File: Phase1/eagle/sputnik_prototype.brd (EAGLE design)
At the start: 100 x 80 mm, 82 parts, among them U1 MEGA128-M, U2 MIC5219 3.3V, Y1 32MHz, Y2 8MHZ

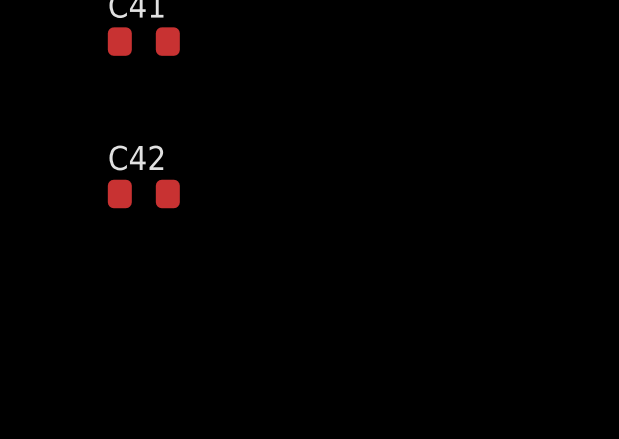
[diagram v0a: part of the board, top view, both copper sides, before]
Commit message: Updated RF schematic
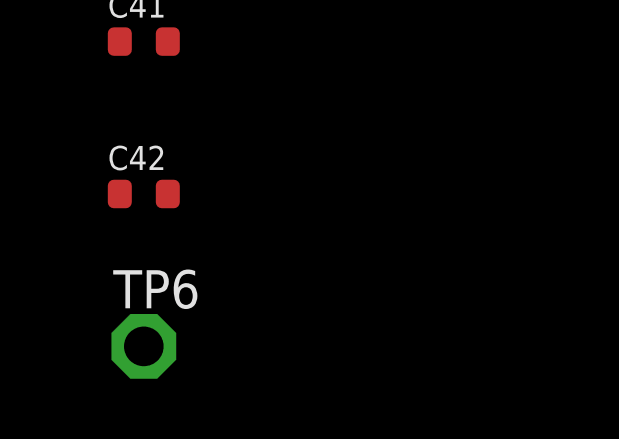
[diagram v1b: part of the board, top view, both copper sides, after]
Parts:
- added TP6: TPSPAD1-13, testpad:P1-13
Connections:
- removed net N$26: C13.1, U$5.2
- removed net N$33: C23.1, C4.1, C6.1, L2.2
- new net N$4: C13.1, L8.1, U$4.6
- new net N$5: C23.1, U$5.8
- net GND: no longer U$4.1
- net N$22: now also U$5.2; no longer U$5.8
- net RFIO: now also C4.1, C6.1, L2.2; no longer L8.1, U$4.6
- net V+: now also TP6.TP
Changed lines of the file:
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@@
 <?xml version="1.0" encoding="utf-8"?>
 <!DOCTYPE eagle SYSTEM "eagle.dtd">
-<eagle version="7.3.0">
+<eagle version="7.5.0">
 <drawing>
 <settings>
@@
 <element name="C41" library="rcl_custom" package=".0603-B-NOSILK" value="100nF" x="-55.88" y="-101.6"/>
 <element name="C42" library="rcl_custom" package=".0603-B-NOSILK" value="470pF" x="-55.88" y="-106.68"/>
+<element name="TP6" library="testpad" package="P1-13" value="TPSPAD1-13" x="-55.88" y="-111.76">
+<attribute name="TP_SIGNAL_NAME" value="" x="-55.88" y="-111.76" size="1.778" layer="27" display="off"/>
+</element>
 </elements>
 <signals>
@@
 <contactref element="U$4" pad="2"/>
 <contactref element="U$4" pad="5"/>
-<contactref element="U$4" pad="1"/>
 <contactref element="C25" pad="2"/>
 <contactref element="C24" pad="2"/>
-<contactref element="U$5" pad="6"/>
 <contactref element="U$5" pad="7"/>
 <contactref element="U$5" pad="9"/>
-<contactref element="U$5" pad="4"/>
 <contactref element="U$5" pad="3"/>
 <contactref element="U$5" pad="1"/>
@@
 <contactref element="U2" pad="2"/>
 <contactref element="C42" pad="1"/>
+<contactref element="U$5" pad="4"/>
+<contactref element="U$5" pad="6"/>
 <wire x1="-56.68" y1="-101.6" x2="-56.68" y2="-106.68" width="0" layer="19" extent="1-1"/>
 <wire x1="-56.68" y1="-96.52" x2="-56.68" y2="-101.6" width="0" layer="19" extent="1-1"/>
@@
 <wire x1="-22.06" y1="48.26" x2="-19.85" y2="44.45" width="0" layer="19" extent="1-1"/>
 <wire x1="-22.86" y1="51.1975" x2="-22.06" y2="48.26" width="0" layer="19" extent="1-1"/>
-<wire x1="-23.51" y1="51.1975" x2="-22.86" y2="51.1975" width="0" layer="19" extent="1-1"/>
 <wire x1="-22.86" y1="52.8725" x2="-22.86" y2="51.1975" width="0" layer="19" extent="1-1"/>
-<wire x1="-25.87" y1="48.26" x2="-23.51" y2="51.1975" width="0" layer="19" extent="1-1"/>
+<wire x1="-25.87" y1="48.26" x2="-22.06" y2="48.26" width="0" layer="19" extent="1-1"/>
 <wire x1="-23.241" y1="32.258" x2="-22.39" y2="36.83" width="0" layer="19" extent="1-1"/>
 <wire x1="-23.241" y1="32.258" x2="-23.241" y2="32.258" width="0" layer="19" extent="1-16"/>
@@
 <contactref element="U2" pad="1"/>
 <contactref element="U2" pad="3"/>
+<contactref element="TP6" pad="TP"/>
+<wire x1="-55.08" y1="-101.6" x2="-55.88" y2="-111.76" width="0" layer="19" extent="1-1"/>
 <wire x1="-56.2" y1="-17.8101" x2="-55.08" y2="-101.6" width="0" layer="19" extent="1-1"/>
 <wire x1="-58.1" y1="-17.8101" x2="-56.2" y2="-17.8101" width="0" layer="19" extent="1-1"/>
@@
 </signal>
 <signal name="N$22">
-<contactref element="U$5" pad="8"/>
 <contactref element="U$6" pad="8"/>
-<wire x1="-27.6614" y1="17.3975" x2="-13.26" y2="40.91" width="0" layer="19" extent="1-1"/>
+<contactref element="U$5" pad="2"/>
+<wire x1="-27.6614" y1="17.3975" x2="-15.22" y2="40.91" width="0" layer="19" extent="1-1"/>
 </signal>
 <signal name="N$24">
@@
 <wire x1="-52.54" y1="48.26" x2="-18.25" y2="48.26" width="0" layer="19" extent="1-1"/>
 </signal>
-<signal name="N$26">
-<contactref element="U$5" pad="2"/>
-<contactref element="C13" pad="1"/>
-<wire x1="-23.66" y1="44.45" x2="-15.22" y2="40.91" width="0" layer="19" extent="1-1"/>
-</signal>
 <signal name="N$27">
 <contactref element="U$4" pad="4"/>
@@
 </signal>
 <signal name="RFIO">
-<contactref element="L8" pad="1"/>
-<contactref element="U$4" pad="6"/>
 <contactref element="U$1" pad="39"/>
-<wire x1="-23.51" y1="52.88" x2="-16.04" y2="52.07" width="0" layer="19" extent="1-1"/>
-<wire x1="-25.88" y1="11.4978" x2="-23.51" y2="52.88" width="0" layer="19" extent="1-1"/>
+<contactref element="C6" pad="1"/>
+<contactref element="C4" pad="1"/>
+<contactref element="L2" pad="2"/>
+<wire x1="-30.01" y1="40.64" x2="-25.88" y2="11.4978" width="0" layer="19" extent="1-1"/>
+<wire x1="-37.63" y1="40.64" x2="-30.01" y2="40.64" width="0" layer="19" extent="1-1"/>
+<wire x1="-33.49" y1="48.26" x2="-30.01" y2="40.64" width="0" layer="19" extent="1-1"/>
 </signal>
 <signal name="RXTX">
@@
 <contactref element="U$2" pad="P$3"/>
 <wire x1="-19.05" y1="32.258" x2="-14.24" y2="39.93" width="0" layer="19" extent="1-1"/>
-</signal>
-<signal name="N$33">
-<contactref element="C6" pad="1"/>
-<contactref element="C4" pad="1"/>
-<contactref element="L2" pad="2"/>
-<contactref element="C23" pad="1"/>
-<wire x1="-30.01" y1="40.64" x2="-19.85" y2="48.26" width="0" layer="19" extent="1-1"/>
-<wire x1="-37.63" y1="40.64" x2="-30.01" y2="40.64" width="0" layer="19" extent="1-1"/>
-<wire x1="-33.49" y1="48.26" x2="-30.01" y2="40.64" width="0" layer="19" extent="1-1"/>
 </signal>
 <signal name="N$29">
@@
 <wire x1="-56.2" y1="-15.2099" x2="-55.08" y2="-106.68" width="0" layer="19" extent="1-1"/>
 </signal>
+<signal name="N$4">
+<contactref element="L8" pad="1"/>
+<contactref element="U$4" pad="6"/>
+<contactref element="C13" pad="1"/>
+<wire x1="-23.51" y1="52.88" x2="-16.04" y2="52.07" width="0" layer="19" extent="1-1"/>
+<wire x1="-23.66" y1="44.45" x2="-23.51" y2="52.88" width="0" layer="19" extent="1-1"/>
+</signal>
+<signal name="N$5">
+<contactref element="C23" pad="1"/>
+<contactref element="U$5" pad="8"/>
+<wire x1="-13.26" y1="40.91" x2="-19.85" y2="48.26" width="0" layer="19" extent="1-1"/>
+</signal>
 </signals>

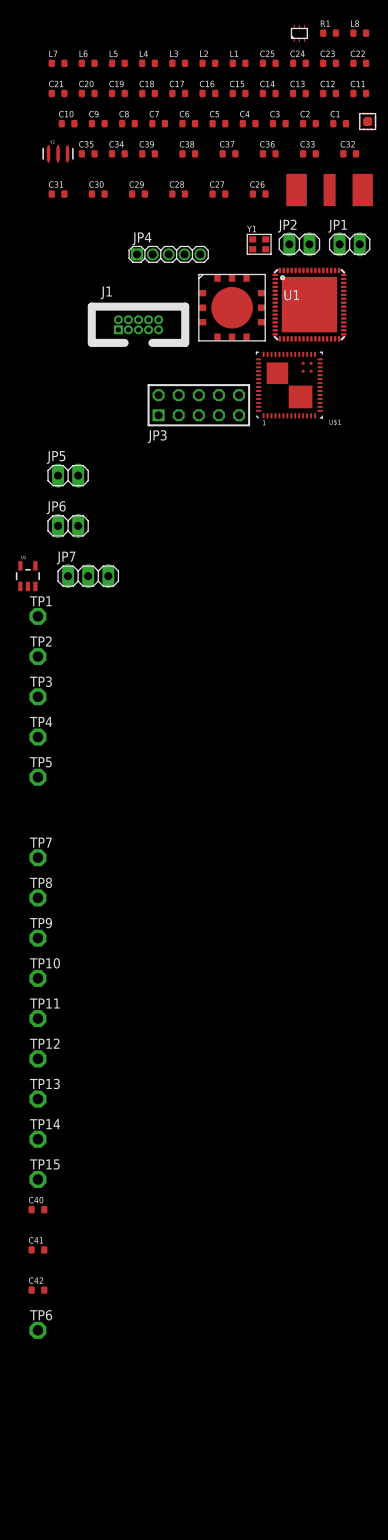
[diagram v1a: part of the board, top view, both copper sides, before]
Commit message: Updated RF schematic
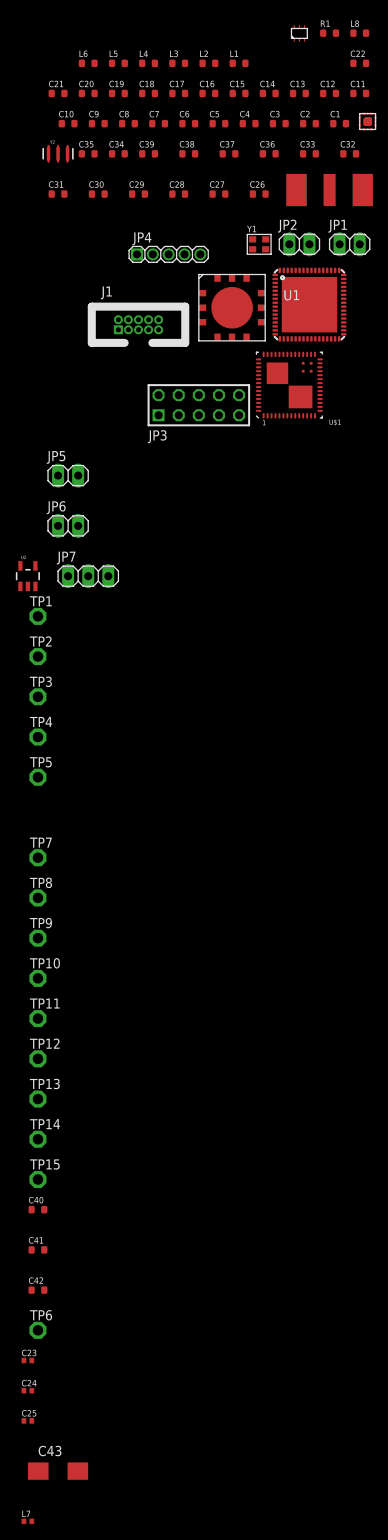
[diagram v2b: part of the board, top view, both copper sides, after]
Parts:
- added C43: 100uF, rcl:CT6032
- C1, C3: value (none) -> 10nF
- C10, C5, C6, C9: value (none) -> 15pF
- C11, C12: value (none) -> 8.2pF
- C13, C14: value (none) -> 100nF
- C15, C17, C19, C22: value (none) -> 10uF
- C16, C18, C20, C21: value (none) -> 0.01uF
- C2, C4: value (none) -> 12pF
- C23, C25: value (none) -> 1nF; device rcl_custom:.0603-B-NOSILK -> rcl_custom:.0402-B-NOSILK
- C24: value (none) -> 10nF; device rcl_custom:.0603-B-NOSILK -> rcl_custom:.0402-B-NOSILK
- C7, C8: value (none) -> 2.2pF
- L1, L2: value (none) -> 22nH
- L3, L4, L5, L6: value (none) -> 15nH
- L7: value (none) -> 24nH; device rcl_custom:.0603-B-NOSILK -> rcl_custom:.0402-B-NOSILK
- L8: value (none) -> 150nH
- R1: value (none) -> 500
- moved L7 184.2 mm to (-57.1, -135.9)
- moved C25 174.1 mm to (-57.1, -123.2)
- moved C24 171.1 mm to (-57.1, -119.4)
- moved C23 168.2 mm to (-57.1, -115.6)
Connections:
- new net N$7: L8.1, U$4.6
- net GND: now also C43.-
- net N$4: now also C25.1; no longer L8.1, U$4.6
- net V+: now also C43.+; no longer C25.1

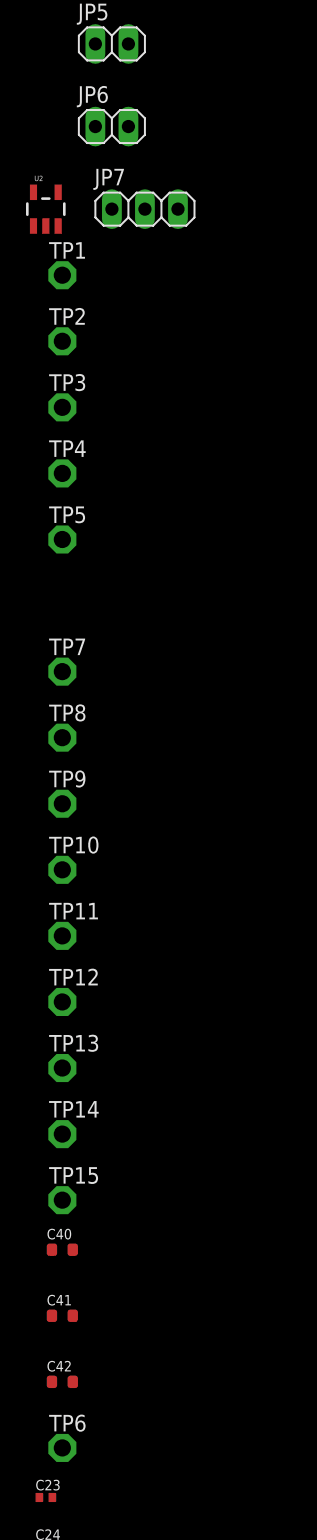
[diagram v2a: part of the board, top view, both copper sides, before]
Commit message: Updated the schematic a bit. Removed I2C line to payload and sense pin
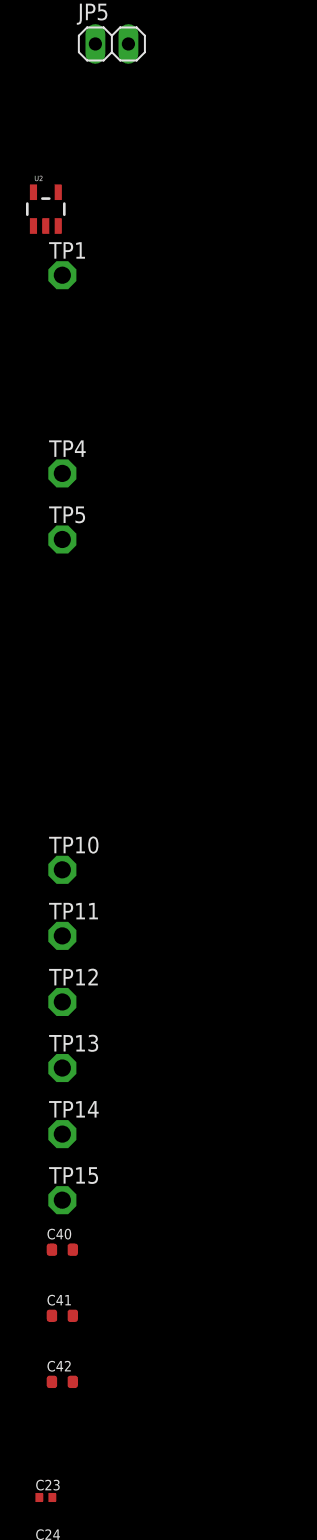
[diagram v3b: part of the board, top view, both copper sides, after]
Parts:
- removed JP6: (no value), psas_c3_team05:1X02
- removed JP7: (no value), pinhead:1X03
- removed TP2, TP3, TP6, TP7, TP8, TP9: TPSPAD1-13, testpad:P1-13
- C23: value 1nF -> (none)
- C24: value 10nF -> (none)
- C43: value 100uF -> (none)
- L7: value 24nH -> (none)
- L8: value 150nH -> (none)
- R1: value 500 -> (none)
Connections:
- net PE4: no longer JP7.1, TP7.TP
- net PE5: no longer JP7.2, TP8.TP
- net PE6: no longer JP7.3, TP9.TP
- net SDA: no longer JP6.2, TP3.TP
- net SDL: no longer JP6.1, TP2.TP
- net V+: no longer TP6.TP
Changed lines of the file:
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@@
 <?xml version="1.0" encoding="utf-8"?>
 <!DOCTYPE eagle SYSTEM "eagle.dtd">
-<eagle version="7.5.0">
+<eagle version="7.4.0">
 <drawing>
 <settings>
@@
 <element name="L5" library="rcl_custom" package=".0603-B-NOSILK" value="15nH" x="-45.72" y="48.26"/>
 <element name="L6" library="rcl_custom" package=".0603-B-NOSILK" value="15nH" x="-49.53" y="48.26"/>
-<element name="L8" library="rcl_custom" package=".0603-B-NOSILK" value="150nH" x="-15.24" y="52.07"/>
-<element name="R1" library="rcl_custom" package=".0603-B-NOSILK" value="500" x="-19.05" y="52.07"/>
+<element name="L8" library="rcl_custom" package=".0603-B-NOSILK" value="" x="-15.24" y="52.07"/>
+<element name="R1" library="rcl_custom" package=".0603-B-NOSILK" value="" x="-19.05" y="52.07"/>
 <element name="U$1" library="psas_c3_team05" package="MKW01Z128" value="MKW01Z128" x="-24.13" y="7.62"/>
 <element name="U$2" library="psas_c3_team05" package="SMAJ716-ND" value="SMAJ716-ND" x="-19.05" y="31.75"/>
@@
 </element>
 <element name="JP5" library="psas_c3_team05" package="1X02" value="" x="-52.07" y="-3.81"/>
-<element name="JP6" library="psas_c3_team05" package="1X02" value="" x="-52.07" y="-10.16"/>
-<element name="JP7" library="pinhead" package="1X03" value="" x="-49.53" y="-16.51"/>
 <element name="U2" library="Lilypad_Arduino_USB_v12" package="SPARKFUN-POWERIC_SOT23-5" value="MIC5219 3.3V" x="-57.15" y="-16.51">
 <attribute name="PROD_ID" value="VREG-09872" x="-57.15" y="-16.51" size="1.778" layer="27" display="off"/>
@@
 <attribute name="TP_SIGNAL_NAME" value="" x="-55.88" y="-21.59" size="1.778" layer="27" display="off"/>
 </element>
-<element name="TP2" library="testpad" package="P1-13" value="TPSPAD1-13" x="-55.88" y="-26.67">
-<attribute name="TP_SIGNAL_NAME" value="" x="-55.88" y="-26.67" size="1.778" layer="27" display="off"/>
-</element>
-<element name="TP3" library="testpad" package="P1-13" value="TPSPAD1-13" x="-55.88" y="-31.75">
-<attribute name="TP_SIGNAL_NAME" value="" x="-55.88" y="-31.75" size="1.778" layer="27" display="off"/>
-</element>
 <element name="TP4" library="testpad" package="P1-13" value="TPSPAD1-13" x="-55.88" y="-36.83">
 <attribute name="TP_SIGNAL_NAME" value="" x="-55.88" y="-36.83" size="1.778" layer="27" display="off"/>
@@
 <element name="TP5" library="testpad" package="P1-13" value="TPSPAD1-13" x="-55.88" y="-41.91">
 <attribute name="TP_SIGNAL_NAME" value="" x="-55.88" y="-41.91" size="1.778" layer="27" display="off"/>
-</element>
-<element name="TP7" library="testpad" package="P1-13" value="TPSPAD1-13" x="-55.88" y="-52.07">
-<attribute name="TP_SIGNAL_NAME" value="" x="-55.88" y="-52.07" size="1.778" layer="27" display="off"/>
-</element>
-<element name="TP8" library="testpad" package="P1-13" value="TPSPAD1-13" x="-55.88" y="-57.15">
-<attribute name="TP_SIGNAL_NAME" value="" x="-55.88" y="-57.15" size="1.778" layer="27" display="off"/>
-</element>
-<element name="TP9" library="testpad" package="P1-13" value="TPSPAD1-13" x="-55.88" y="-62.23">
-<attribute name="TP_SIGNAL_NAME" value="" x="-55.88" y="-62.23" size="1.778" layer="27" display="off"/>
 </element>
 <element name="TP10" library="testpad" package="P1-13" value="TPSPAD1-13" x="-55.88" y="-67.31">
@@
 <element name="C41" library="rcl_custom" package=".0603-B-NOSILK" value="100nF" x="-55.88" y="-101.6"/>
 <element name="C42" library="rcl_custom" package=".0603-B-NOSILK" value="470pF" x="-55.88" y="-106.68"/>
-<element name="TP6" library="testpad" package="P1-13" value="TPSPAD1-13" x="-55.88" y="-111.76">
-<attribute name="TP_SIGNAL_NAME" value="" x="-55.88" y="-111.76" size="1.778" layer="27" display="off"/>
-</element>
-<element name="C23" library="rcl_custom" package=".0402-B-NOSILK" value="1nF" x="-57.15" y="-115.57"/>
-<element name="C24" library="rcl_custom" package=".0402-B-NOSILK" value="10nF" x="-57.15" y="-119.38"/>
+<element name="C23" library="rcl_custom" package=".0402-B-NOSILK" value="" x="-57.15" y="-115.57"/>
+<element name="C24" library="rcl_custom" package=".0402-B-NOSILK" value="" x="-57.15" y="-119.38"/>
 <element name="C25" library="rcl_custom" package=".0402-B-NOSILK" value="1nF" x="-57.15" y="-123.19"/>
-<element name="C43" library="rcl" package="CT6032" value="100uF" x="-53.34" y="-129.54"/>
-<element name="L7" library="rcl_custom" package=".0402-B-NOSILK" value="24nH" x="-57.15" y="-135.89"/>
+<element name="C43" library="rcl" package="CT6032" value="" x="-53.34" y="-129.54"/>
+<element name="L7" library="rcl_custom" package=".0402-B-NOSILK" value="" x="-57.15" y="-135.89"/>
 </elements>
 <signals>
@@
 <contactref element="U2" pad="1"/>
 <contactref element="U2" pad="3"/>
-<contactref element="TP6" pad="TP"/>
 <contactref element="U$6" pad="11"/>
 <contactref element="C24" pad="1"/>
 <contactref element="C43" pad="+"/>
 <wire x1="-57.65" y1="-119.38" x2="-55.84" y2="-129.54" width="0" layer="19" extent="1-1"/>
-<wire x1="-55.88" y1="-111.76" x2="-57.65" y2="-119.38" width="0" layer="19" extent="1-1"/>
-<wire x1="-55.08" y1="-101.6" x2="-55.88" y2="-111.76" width="0" layer="19" extent="1-1"/>
+<wire x1="-55.08" y1="-101.6" x2="-57.65" y2="-119.38" width="0" layer="19" extent="1-1"/>
 <wire x1="-56.2" y1="-17.8101" x2="-55.08" y2="-101.6" width="0" layer="19" extent="1-1"/>
 <wire x1="-58.1" y1="-17.8101" x2="-56.2" y2="-17.8101" width="0" layer="19" extent="1-1"/>
@@
 <contactref element="JP2" pad="1"/>
 <contactref element="U1" pad="25"/>
-<contactref element="JP6" pad="1"/>
-<contactref element="TP2" pad="TP"/>
-<wire x1="-53.34" y1="-10.16" x2="-55.88" y2="-26.67" width="0" layer="19" extent="1-1"/>
-<wire x1="-21.34" y1="13.455" x2="-53.34" y2="-10.16" width="0" layer="19" extent="1-1"/>
 <wire x1="-24.13" y1="25.4" x2="-21.34" y2="13.455" width="0" layer="19" extent="1-1"/>
 </signal>
@@
 <contactref element="JP2" pad="2"/>
 <contactref element="U1" pad="26"/>
-<contactref element="JP6" pad="2"/>
-<contactref element="TP3" pad="TP"/>
-<wire x1="-50.8" y1="-10.16" x2="-55.88" y2="-31.75" width="0" layer="19" extent="1-1"/>
-<wire x1="-20.84" y1="13.455" x2="-50.8" y2="-10.16" width="0" layer="19" extent="1-1"/>
 <wire x1="-21.59" y1="25.4" x2="-20.84" y2="13.455" width="0" layer="19" extent="1-1"/>
 </signal>
@@
 <signal name="PE4">
 <contactref element="U1" pad="6"/>
-<contactref element="JP7" pad="1"/>
-<contactref element="TP7" pad="TP"/>
-<wire x1="-52.07" y1="-16.51" x2="-55.88" y2="-52.07" width="0" layer="19" extent="1-1"/>
-<wire x1="-25.915" y1="19.03" x2="-52.07" y2="-16.51" width="0" layer="19" extent="1-1"/>
 </signal>
 <signal name="PE5">
 <contactref element="U1" pad="7"/>
-<contactref element="JP7" pad="2"/>
-<contactref element="TP8" pad="TP"/>
-<wire x1="-49.53" y1="-16.51" x2="-55.88" y2="-57.15" width="0" layer="19" extent="1-1"/>
-<wire x1="-25.915" y1="18.53" x2="-49.53" y2="-16.51" width="0" layer="19" extent="1-1"/>
 </signal>
 <signal name="PE6">
 <contactref element="U1" pad="8"/>
-<contactref element="JP7" pad="3"/>
-<contactref element="TP9" pad="TP"/>
-<wire x1="-46.99" y1="-16.51" x2="-55.88" y2="-62.23" width="0" layer="19" extent="1-1"/>
-<wire x1="-25.915" y1="18.03" x2="-46.99" y2="-16.51" width="0" layer="19" extent="1-1"/>
 </signal>
 <signal name="3.3V">
